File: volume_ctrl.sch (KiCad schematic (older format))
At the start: 40 parts, among them U1 TL072, U2 NE5532, U3 NE5532, U4 THAT2180

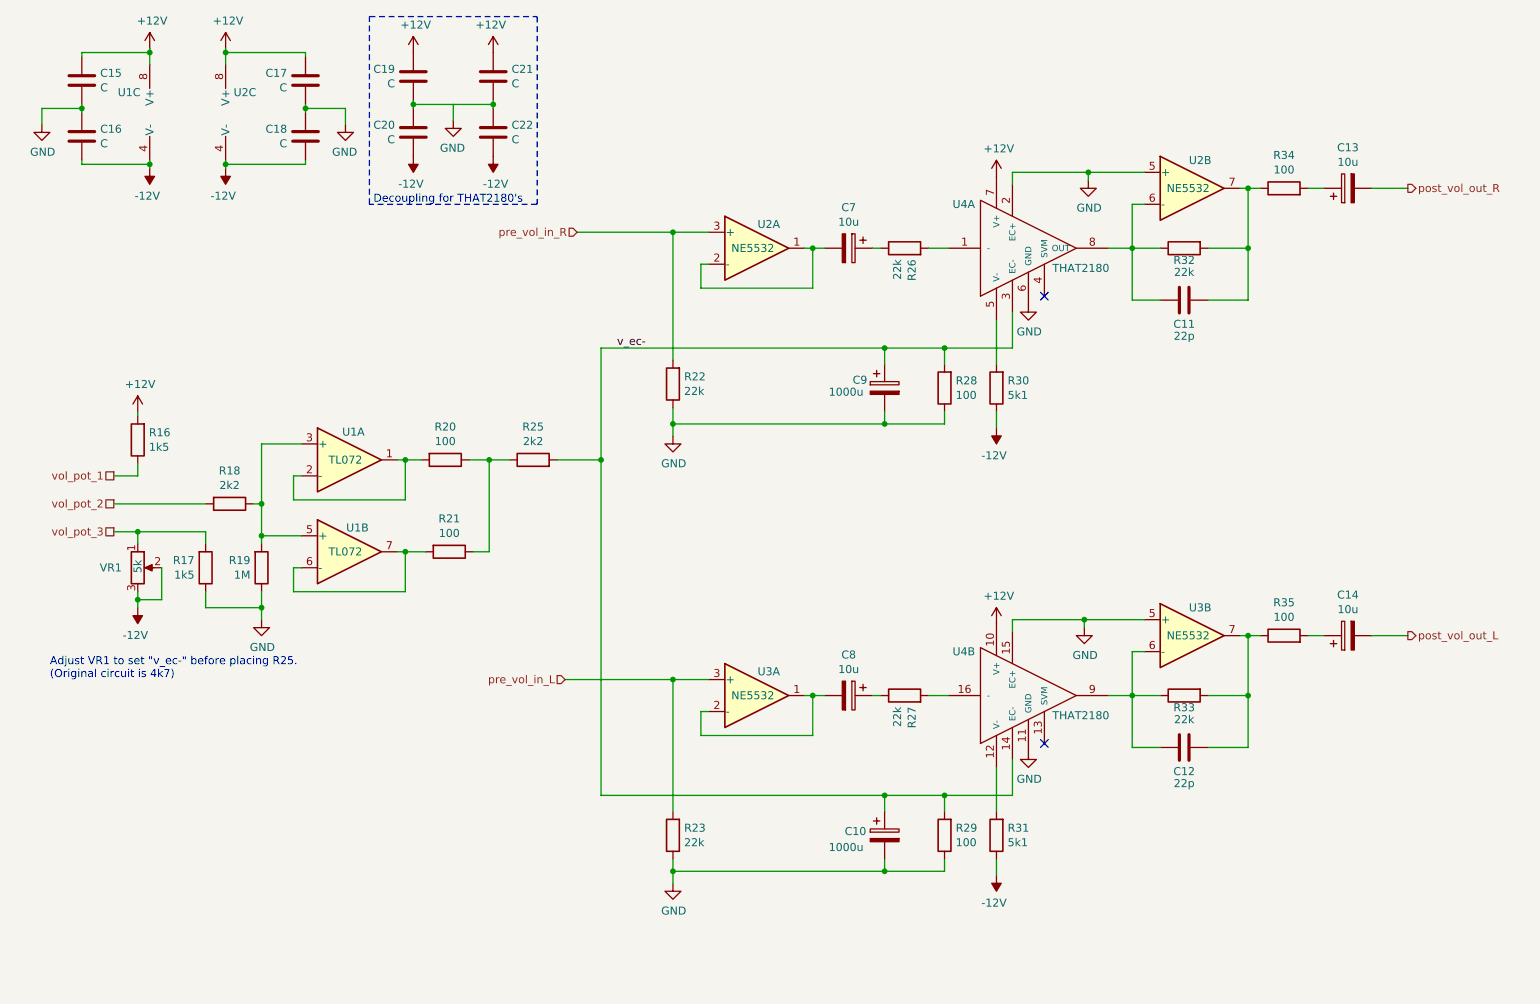
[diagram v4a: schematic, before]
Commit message: Fixed several DRC errors. Tied audoi input returns to GND. Added Switch logic.
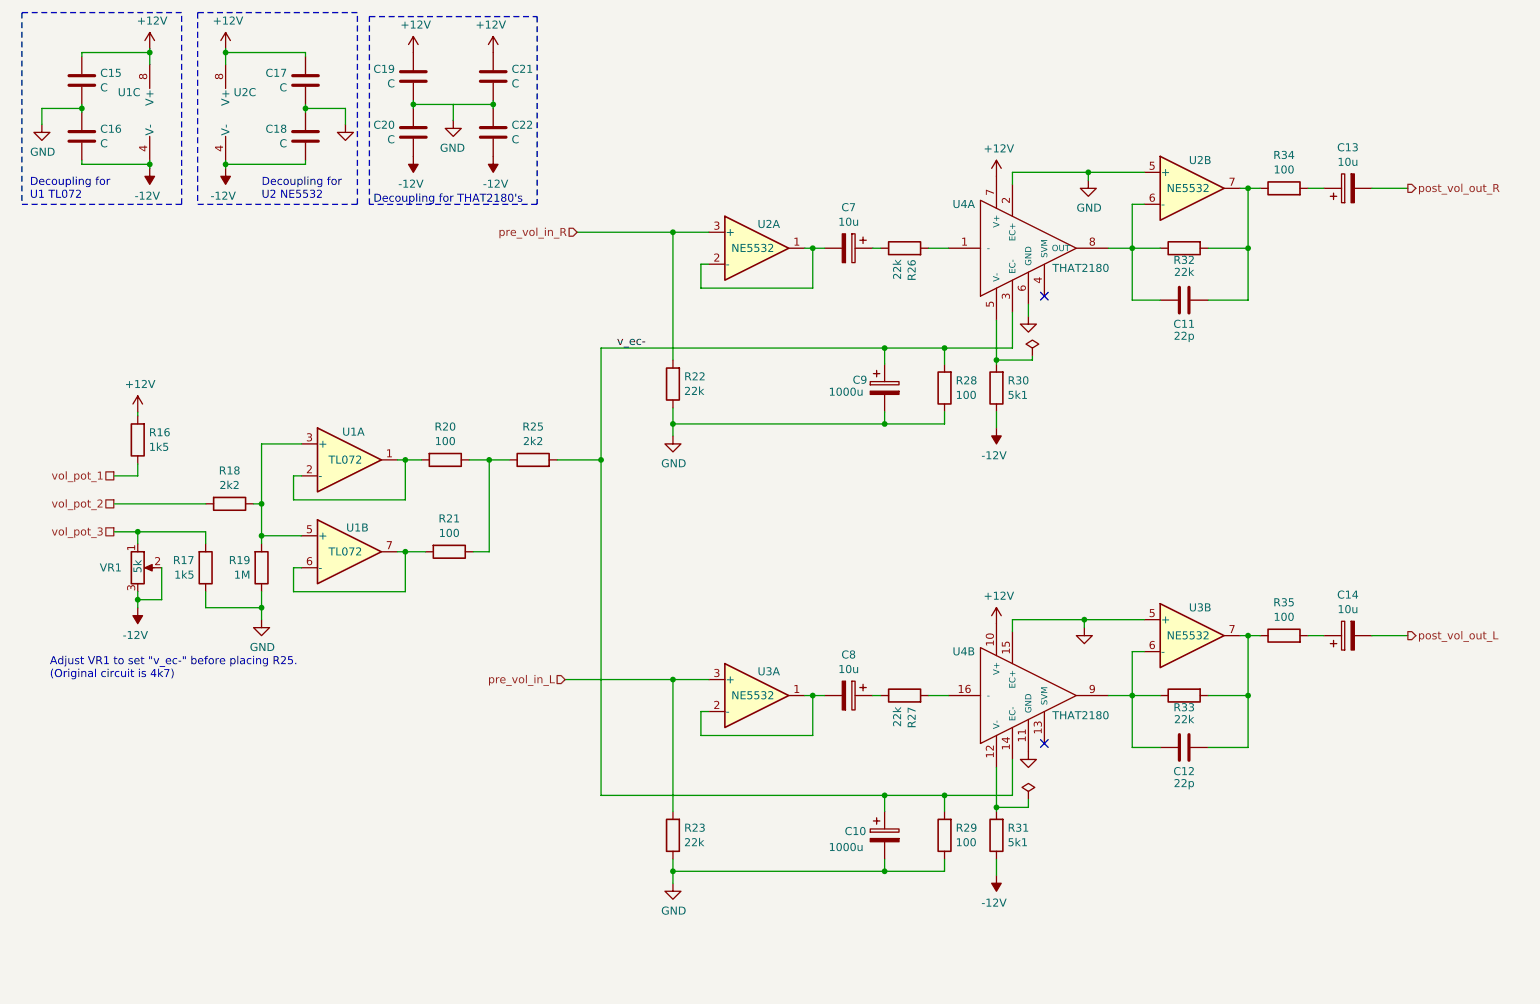
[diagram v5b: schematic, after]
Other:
- note added: "Decoupling for \nU1 TL072"
- note added: "Decoupling for \nU2 NE5532"
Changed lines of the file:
@@
 EESchema Schematic File Version 4
+LIBS:AAMB-cache
 EELAYER 30 0
 EELAYER END
@@
 	-1   0    0    1
 $EndComp
-$Comp
-L power:GND #PWR025
-U 1 1 5E27BE60
-P 6875 5125
-F 0 "#PWR025" H 6875 4875 50  0001 C CNN
-F 1 "GND" H 6880 4952 50  0000 C CNN
-F 2 "" H 6875 5125 50  0001 C CNN
-F 3 "" H 6875 5125 50  0001 C CNN
-	1    6875 5125
-	1    0    0    -1
-$EndComp
-$Comp
-L power:GND #PWR027
-U 1 1 5E27C409
-P 7225 4350
-F 0 "#PWR027" H 7225 4100 50  0001 C CNN
-F 1 "GND" H 7230 4177 50  0000 C CNN
-F 2 "" H 7225 4350 50  0001 C CNN
-F 3 "" H 7225 4350 50  0001 C CNN
-	1    7225 4350
-	1    0    0    -1
-$EndComp
 Wire Wire Line
 	6775 4375 6775 4300
-Wire Wire Line
-	6775 4300 7225 4300
-Wire Wire Line
-	7225 4300 7225 4350
 $Comp
 L Amplifier_Operational:NE5532 U3
@@
 	6675 5900 6675 5800
 Wire Wire Line
-	6675 5500 6675 5225
+	6675 5500 6675 5475
 $Comp
 L Device:R R29
@@
 Wire Wire Line
 	7375 4775 7525 4775
-Wire Wire Line
-	7225 4300 7600 4300
-Connection ~ 7225 4300
 Text HLabel 9250 4400 2    50   Output ~ 0
 post_vol_out_L
@@
 $EndComp
 $Comp
-L power:GND #PWR024
-U 1 1 5E3A8EAA
-P 6875 2325
-F 0 "#PWR024" H 6875 2075 50  0001 C CNN
-F 1 "GND" H 6880 2152 50  0000 C CNN
-F 2 "" H 6875 2325 50  0001 C CNN
-F 3 "" H 6875 2325 50  0001 C CNN
-	1    6875 2325
-	1    0    0    -1
-$EndComp
-$Comp
 L power:GND #PWR026
 U 1 1 5E3A8EB0
@@
 	6675 3100 6675 3000
 Wire Wire Line
-	6675 2700 6675 2425
+	6675 2700 6675 2675
 $Comp
 L Device:R R28
@@
 $EndComp
 Wire Wire Line
-	2350 750  2350 775
-Wire Wire Line
-	2350 1125 2350 1100
-Wire Wire Line
-	2350 1100 2600 1100
-Wire Wire Line
-	2600 1100 2600 1200
-Connection ~ 2350 1100
-Wire Wire Line
-	2350 1100 2350 1075
-$Comp
-L power:GND #PWR029
-U 1 1 5E4ED35C
-P 2600 1200
-F 0 "#PWR029" H 2600 950 50  0001 C CNN
-F 1 "GND" H 2605 1027 50  0000 C CNN
-F 2 "" H 2600 1200 50  0001 C CNN
-F 3 "" H 2600 1200 50  0001 C CNN
-	1    2600 1200
-	-1   0    0    -1
-$EndComp
-Wire Wire Line
 	2350 1450 2350 1425
 Wire Wire Line
-	1850 725  1850 750
-Wire Wire Line
-	1850 1425 1850 1450
-Wire Wire Line
-	2350 750  1850 750
-Connection ~ 1850 750
-Wire Wire Line
-	1850 750  1850 825
-Wire Wire Line
 	2350 1450 1850 1450
-Connection ~ 1850 1450
 Wire Wire Line
 	1850 1450 1850 1475
@@
 Text Notes 2775 1700 0    50   ~ 0
 Decoupling for THAT2180's
+Wire Wire Line
+	1850 1425 1850 1450
+Connection ~ 1850 1450
+Wire Wire Line
+	1850 725  1850 750
+Wire Wire Line
+	2350 775  2350 750
+Wire Wire Line
+	2350 750  1850 750
+Connection ~ 1850 750
+Wire Wire Line
+	1850 750  1850 825
+$Comp
+L power:GND #PWR0114
+U 1 1 5E322682
+P 6875 2400
+F 0 "#PWR0114" H 6875 2150 50  0001 C CNN
+F 1 "GND" H 6875 2250 50  0001 C CNN
+F 2 "" H 6875 2400 50  0001 C CNN
+F 3 "" H 6875 2400 50  0001 C CNN
+	1    6875 2400
+	1    0    0    -1
+$EndComp
+Wire Wire Line
+	6875 2325 6875 2400
+$Comp
+L power:GND #PWR0117
+U 1 1 5E32CB65
+P 2600 1200
+F 0 "#PWR0117" H 2600 950 50  0001 C CNN
+F 1 "GND" H 2600 1050 50  0001 C CNN
+F 2 "" H 2600 1200 50  0001 C CNN
+F 3 "" H 2600 1200 50  0001 C CNN
+	1    2600 1200
+	1    0    0    -1
+$EndComp
+Wire Wire Line
+	2600 1200 2600 1100
+Wire Wire Line
+	2600 1100 2350 1100
+Wire Wire Line
+	2350 1100 2350 1125
+Wire Wire Line
+	2350 1075 2350 1100
+Connection ~ 2350 1100
+Wire Wire Line
+	6775 4300 7225 4300
+$Comp
+L power:GND #PWR0119
+U 1 1 5E34434F
+P 7225 4350
+F 0 "#PWR0119" H 7225 4100 50  0001 C CNN
+F 1 "GND" H 7225 4200 50  0001 C CNN
+F 2 "" H 7225 4350 50  0001 C CNN
+F 3 "" H 7225 4350 50  0001 C CNN
+	1    7225 4350
+	1    0    0    -1
+$EndComp
+Wire Wire Line
+	7225 4350 7225 4300
+Connection ~ 7225 4300
+Wire Wire Line
+	7225 4300 7600 4300
+$Comp
+L power:GND #PWR0122
+U 1 1 5E366A48
+P 6875 5125
+F 0 "#PWR0122" H 6875 4875 50  0001 C CNN
+F 1 "GND" H 6875 4975 50  0001 C CNN
+F 2 "" H 6875 5125 50  0001 C CNN
+F 3 "" H 6875 5125 50  0001 C CNN
+	1    6875 5125
+	1    0    0    -1
+$EndComp
+$Comp
+L power:PWR_FLAG #FLG?
+U 1 1 5E36AD8D
+P 6900 2650
+AR Path="/5E36AD8D" Ref="#FLG?"  Part="1"
+AR Path="/5E227FCE/5E36AD8D" Ref="#FLG0106"  Part="1"
+F 0 "#FLG0106" H 6900 2725 50  0001 C CNN
+F 1 "PWR_FLAG" H 6900 2824 50  0001 C CNN
+F 2 "" H 6900 2650 50  0001 C CNN
+F 3 "~" H 6900 2650 50  0001 C CNN
+	1    6900 2650
+	1    0    0    -1
+$EndComp
+Wire Wire Line
+	6900 2650 6900 2675
+Wire Wire Line
+	6900 2675 6675 2675
+Connection ~ 6675 2675
+Wire Wire Line
+	6675 2675 6675 2425
+$Comp
+L power:PWR_FLAG #FLG?
+U 1 1 5E378F4C
+P 6875 5425
+AR Path="/5E378F4C" Ref="#FLG?"  Part="1"
+AR Path="/5E227FCE/5E378F4C" Ref="#FLG0107"  Part="1"
+F 0 "#FLG0107" H 6875 5500 50  0001 C CNN
+F 1 "PWR_FLAG" H 6875 5599 50  0001 C CNN
+F 2 "" H 6875 5425 50  0001 C CNN
+F 3 "~" H 6875 5425 50  0001 C CNN
+	1    6875 5425
+	1    0    0    -1
+$EndComp
+Wire Wire Line
+	6875 5425 6875 5475
+Wire Wire Line
+	6875 5475 6675 5475
+Connection ~ 6675 5475
+Wire Wire Line
+	6675 5475 6675 5225
+Wire Notes Line
+	1675 500  1675 1700
+Wire Notes Line
+	1675 1700 2675 1700
+Wire Notes Line
+	2675 1700 2675 500
+Wire Notes Line
+	2675 500  1675 500
+Wire Notes Line
+	1575 500  575  500
+Wire Notes Line
+	575  500  575  1700
+Wire Notes Line
+	575  1700 1575 1700
+Wire Notes Line
+	1575 1700 1575 500
+Text Notes 2075 1675 0    50   ~ 0
+Decoupling for \nU2 NE5532
+Text Notes 625  1675 0    50   ~ 0
+Decoupling for \nU1 TL072
 $EndSCHEMATC

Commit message: Added test points. Schematic cleanup.
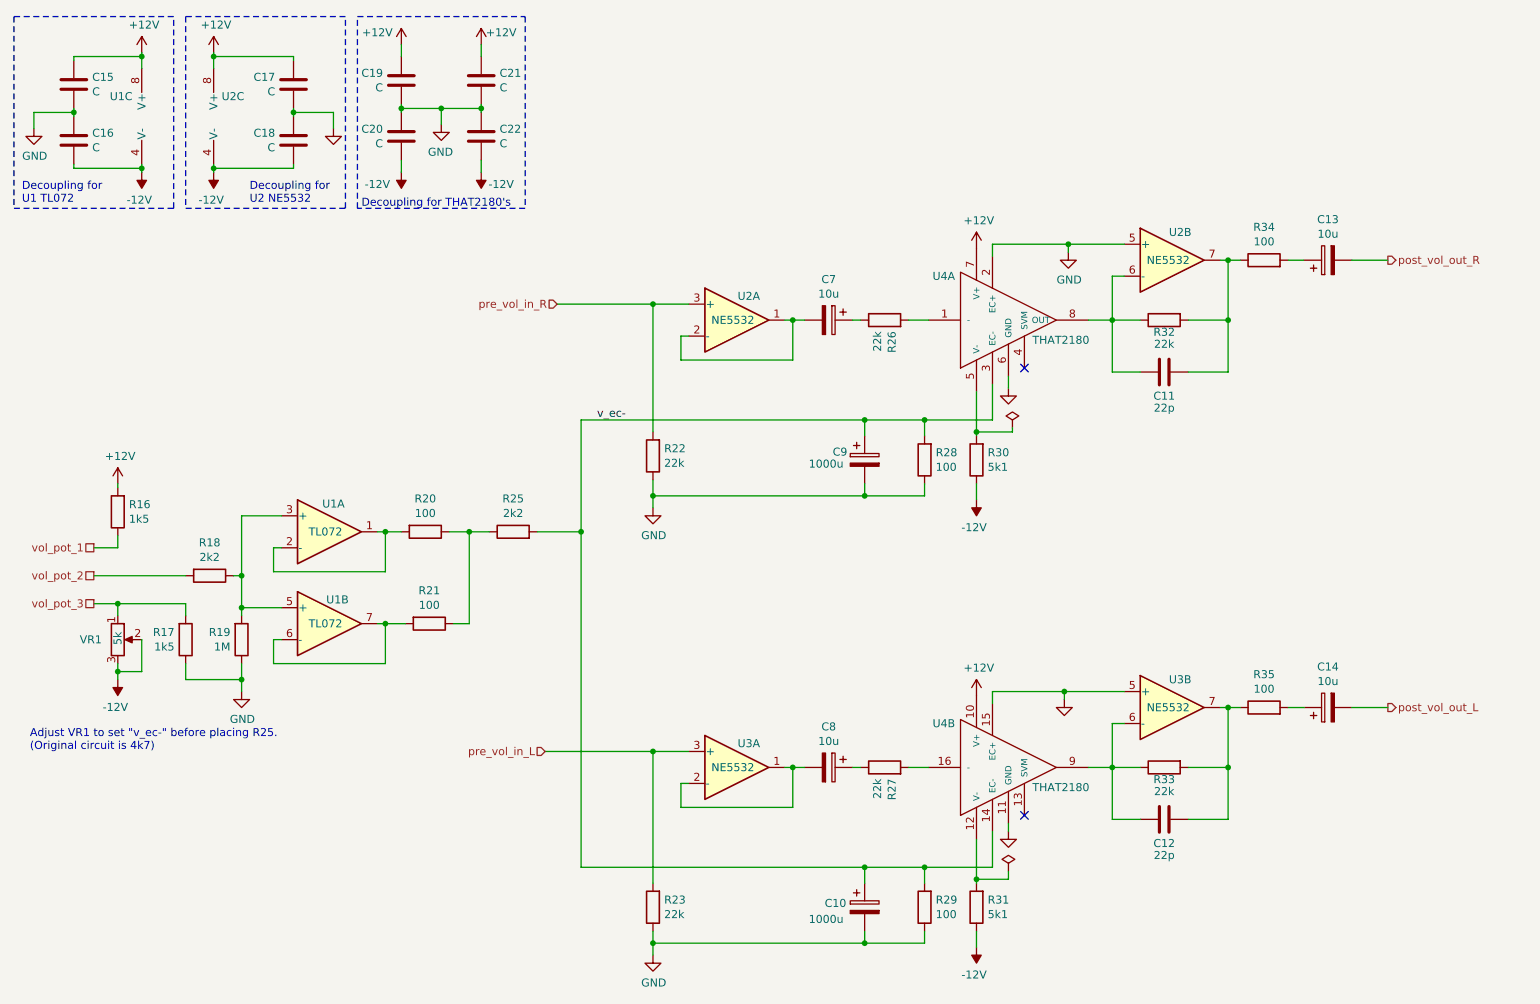
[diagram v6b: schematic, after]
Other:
- moved on the sheet: C10, C11, C12, C13, C14, C15, C16, C17, C18, C19, C20, C21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

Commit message: Cleaning up user configs.
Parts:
- C10, C9: footprint (none) -> Capacitor_SMD:C_Elec_10x10.2; DigiKey (none) -> https://www.digikey.com/product-detail/en/panasonic-electro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
- C11, C12: footprint (none) -> Capacitor_SMD:C_0603_1608Metric_Pad1.05x0.95mm_HandSolder
- C13, C14, C7, C8: footprint (none) -> Capacitor_THT:CP_Radial_D5.0mm_P2.00mm
- C15, C16, C17, C18, C19, C20, C21, C22: value C -> 0.1u; footprint (none) -> Capacitor_SMD:C_0603_1608Metric_Pad1.05x0.95mm_HandSolder; DigiKey (none) -> https://www.digikey.com/product-detail/en/kemet/C0603C104Z3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
- R16, R17, R18, R19, R20, R21, R22, R23, R25, R26, R27, R28, R29, R30, R31, R32, R33, R34, R35: footprint (none) -> Resistor_SMD:R_0603_1608Metric_Pad1.05x0.95mm_HandSolder
- U4: DigiKey (none) -> https://www.digikey.com/product-detail/en/mill-max-manufact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
- VR1: Mouser (none) -> https://www.mouser.com/ProductDetail/Bourns/PV36W502C01B00?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
